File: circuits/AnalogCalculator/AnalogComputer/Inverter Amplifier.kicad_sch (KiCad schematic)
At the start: 9 parts, among them U7 LM324

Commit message: update circuits
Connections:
- net +12V renamed VCC
- net -12V renamed VSS
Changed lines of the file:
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@@
     (effects (font (size 1.27 1.27)) (justify right))
-  )
-  (symbol (lib_id "power:-12V") (at 205.74 59.69 0) (unit 1)
-    (in_bom yes) (on_board yes) (dnp no) (fields_autoplaced)
-    (property "Reference" "#PWR020" (at 205.74 57.15 0)
-      (effects (font (size 1.27 1.27)) hide)
-    )
-    (property "Value" "-12V" (at 205.74 56.1142 0)
-      (effects (font (size 1.27 1.27)))
-    )
-    (property "Footprint" "" (at 205.74 59.69 0)
-      (effects (font (size 1.27 1.27)) hide)
-    )
-    (property "Datasheet" "" (at 205.74 59.69 0)
-      (effects (font (size 1.27 1.27)) hide)
-    )
-    (pin "1")
-    (instances
-      (project "AnalogComputer"
-        (path "/923be781-3164-4152-815e-8f20a1ba1c2e/2eaadc53-ec8e-4601-8972-28fb767e7b1c"
-          (reference "#PWR020") (unit 1)
-        )
-        (path "/923be781-3164-4152-815e-8f20a1ba1c2e/35385f48-c3af-4985-ac23-c22d34684f12"
-          (reference "#PWR023") (unit 1)
-        )
-        (path "/923be781-3164-4152-815e-8f20a1ba1c2e/f6e088c9-b3e2-442b-a6da-db81b116fe83"
-          (reference "#PWR026") (unit 1)
-        )
-      )
-    )
   )
   (symbol (lib_id "Amplifier_Operational:LM324") (at 193.04 78.74 0) (unit 5)
@@
     )
   )
+  (symbol (lib_id "power:VSS") (at 205.74 59.69 0) (unit 1)
+    (in_bom yes) (on_board yes) (dnp no) (fields_autoplaced)
+    (property "Reference" "#PWR023" (at 205.74 63.5 0)
+      (effects (font (size 1.27 1.27)) hide)
+    )
+    (property "Value" "VSS" (at 205.74 56.1881 0)
+      (effects (font (size 1.27 1.27)))
+    )
+    (property "Footprint" "" (at 205.74 59.69 0)
+      (effects (font (size 1.27 1.27)) hide)
+    )
+    (property "Datasheet" "" (at 205.74 59.69 0)
+      (effects (font (size 1.27 1.27)) hide)
+    )
+    (pin "1")
+    (instances
+      (project "AnalogComputer"
+        (path "/923be781-3164-4152-815e-8f20a1ba1c2e/2eaadc53-ec8e-4601-8972-28fb767e7b1c"
+          (reference "#PWR023") (unit 1)
+        )
+        (path "/923be781-3164-4152-815e-8f20a1ba1c2e/35385f48-c3af-4985-ac23-c22d34684f12"
+          (reference "#PWR025") (unit 1)
+        )
+        (path "/923be781-3164-4152-815e-8f20a1ba1c2e/f6e088c9-b3e2-442b-a6da-db81b116fe83"
+          (reference "#PWR026") (unit 1)
+        )
+      )
+    )
+  )
   (symbol (lib_id "Amplifier_Operational:LM324") (at 78.74 78.74 0) (unit 1)
     (in_bom yes) (on_board yes) (dnp no) (fields_autoplaced)
@@
     )
   )
-  (symbol (lib_id "power:+12V") (at 190.5 59.69 0) (unit 1)
+  (symbol (lib_id "power:VCC") (at 190.5 59.69 0) (unit 1)
     (in_bom yes) (on_board yes) (dnp no) (fields_autoplaced)
     (property "Reference" "#PWR019" (at 190.5 63.5 0)
       (effects (font (size 1.27 1.27)) hide)
     )
-    (property "Value" "+12V" (at 190.5 56.1142 0)
+    (property "Value" "VCC" (at 190.5 56.1881 0)
       (effects (font (size 1.27 1.27)))
     )
@@
         )
         (path "/923be781-3164-4152-815e-8f20a1ba1c2e/35385f48-c3af-4985-ac23-c22d34684f12"
+          (reference "#PWR020") (unit 1)
+        )
+        (path "/923be781-3164-4152-815e-8f20a1ba1c2e/f6e088c9-b3e2-442b-a6da-db81b116fe83"
           (reference "#PWR022") (unit 1)
         )
-        (path "/923be781-3164-4152-815e-8f20a1ba1c2e/f6e088c9-b3e2-442b-a6da-db81b116fe83"
-          (reference "#PWR025") (unit 1)
-        )
-      )
+      )

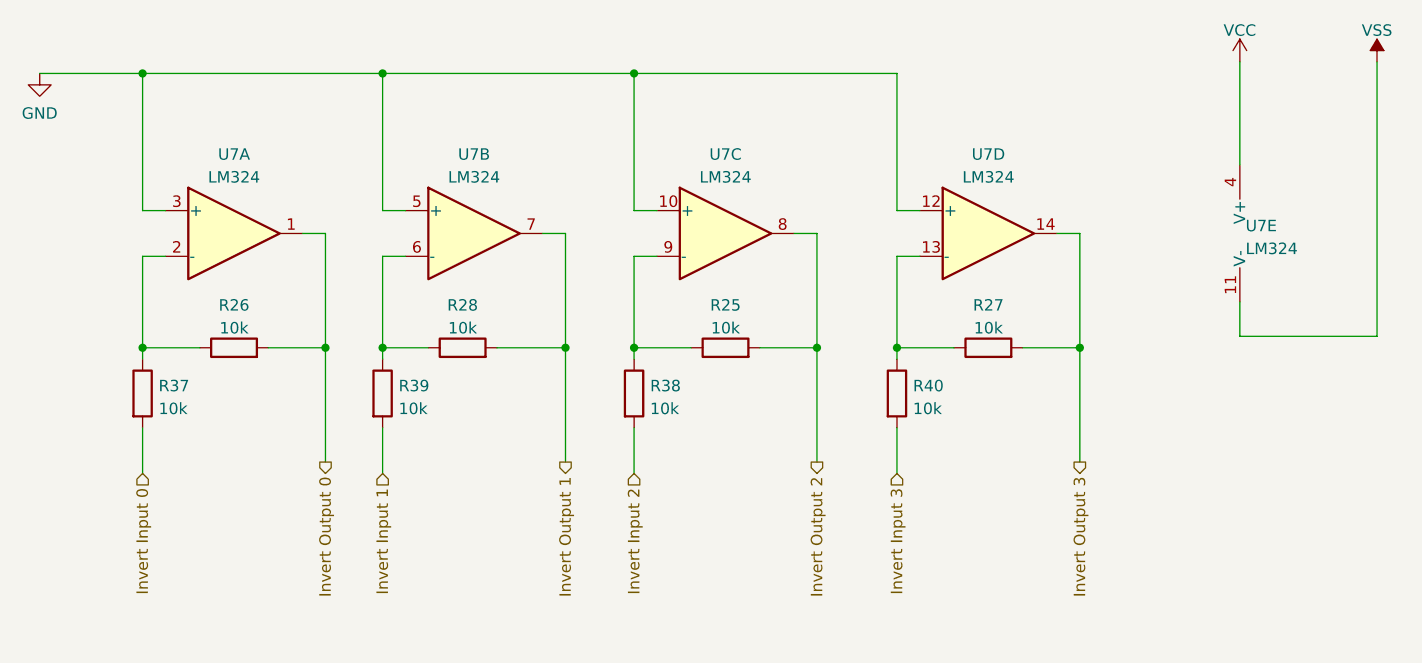
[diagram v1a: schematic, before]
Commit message: update analog computer layout
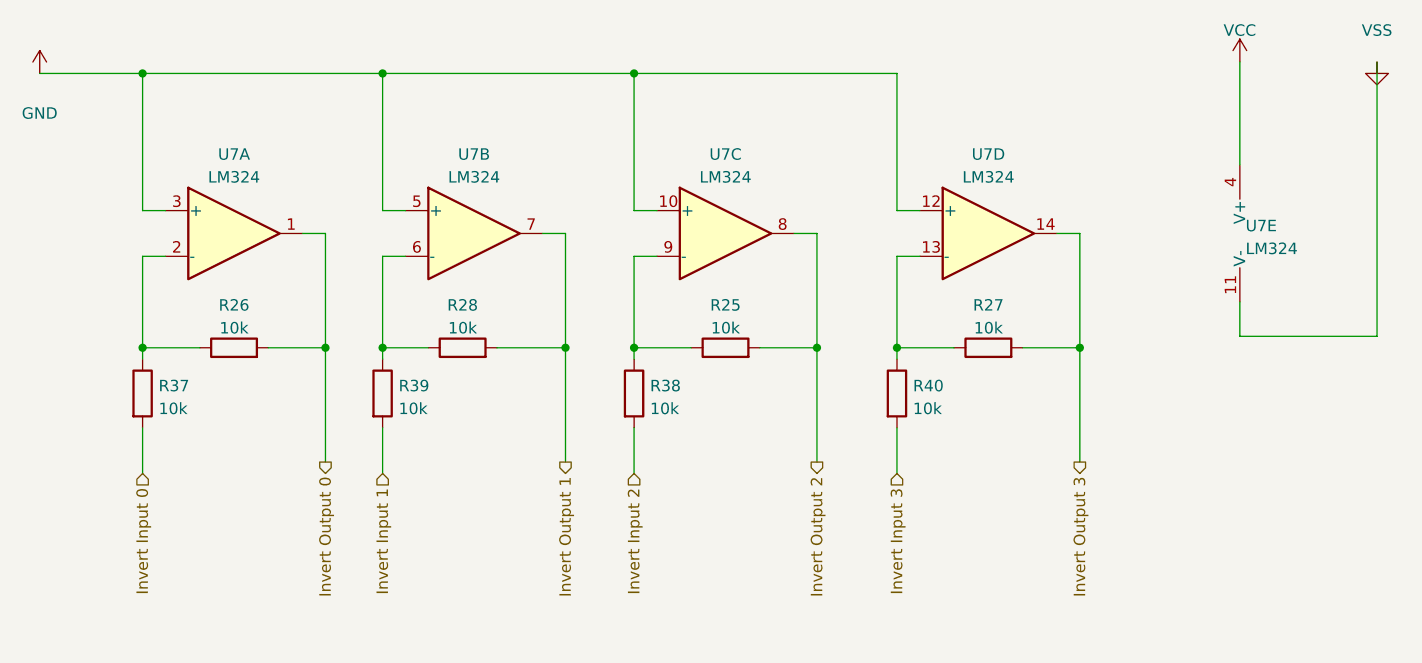
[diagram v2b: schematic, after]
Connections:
- net VSS is gone; now on net GND: U7.11 (V-)
- net GND: no longer U7.10 (+), U7.12 (+), U7.3 (+), U7.5 (+)
- new net VDD: U7.10 (+), U7.12 (+), U7.3 (+), U7.5 (+)
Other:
- company: (none) -> Out-of-band Development, LLC
- title: (none) -> Analog Computer
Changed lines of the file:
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@@
 (kicad_sch (version 20230121) (generator eeschema)
   (paper "A4")
+  (title_block
+    (title "Analog Computer")
+    (date "2023-03-08")
+    (rev "v1")
+    (company "Out-of-band Development, LLC")
+    (comment 1 "Matthew Whited")
+    (comment 2 "Inverting Amplifier")
+  )
   (junction (at 123.19 91.44) (diameter 0) (color 0 0 0 0)
   )
@@
     )
   )
-  (symbol (lib_id "power:VSS") (at 205.74 59.69 0) (unit 1)
+  (symbol (lib_id "power:GND") (at 205.74 59.69 0) (unit 1)
     (in_bom yes) (on_board yes) (dnp no) (fields_autoplaced)
     (property "Reference" "#PWR023" (at 205.74 63.5 0)
@@
     )
   )
-  (symbol (lib_id "power:GND") (at 57.15 60.96 0) (unit 1)
+  (symbol (lib_id "power:VDD") (at 57.15 60.96 0) (unit 1)
     (in_bom yes) (on_board yes) (dnp no) (fields_autoplaced)
     (property "Reference" "#PWR021" (at 57.15 67.31 0)
